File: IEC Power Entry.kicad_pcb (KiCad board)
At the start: 2 copper layers, 64.5 x 70.2 mm, 13 parts, among them J1 Transformer Primary, P1 MountingHole_Pad, P2 Earth

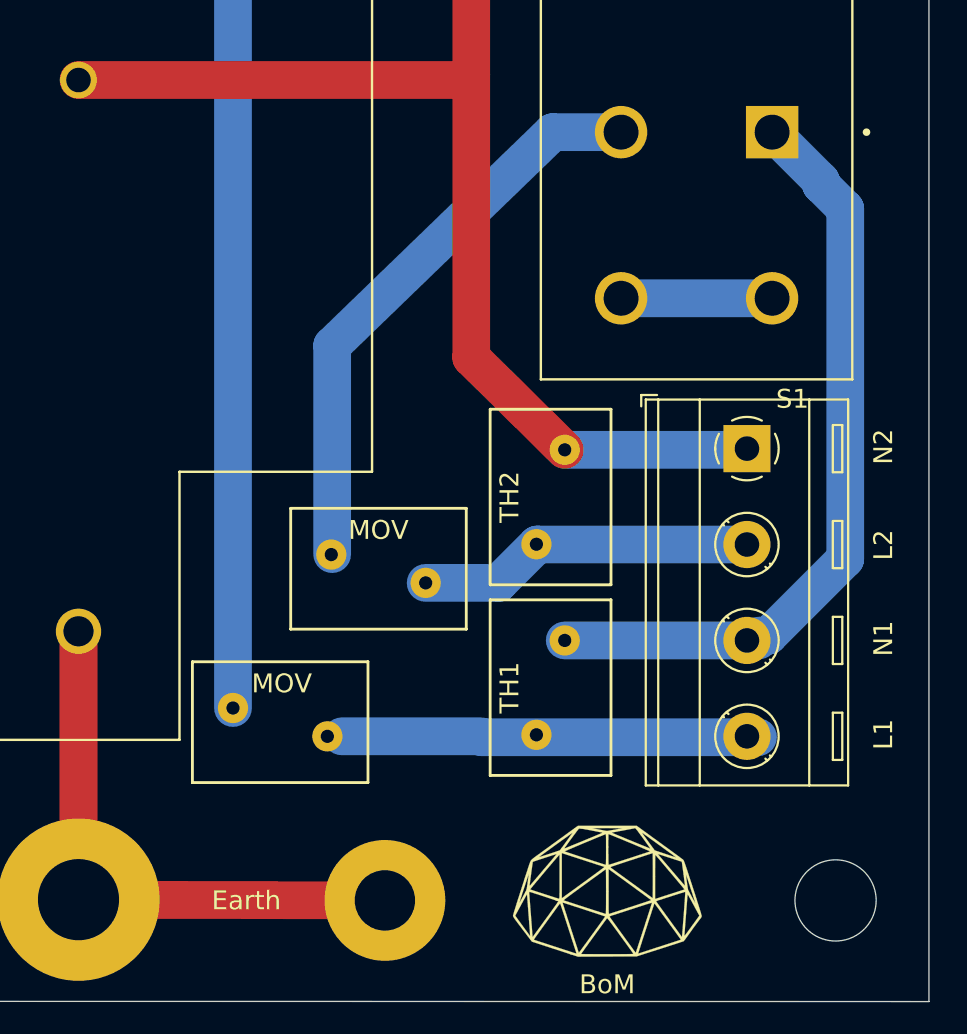
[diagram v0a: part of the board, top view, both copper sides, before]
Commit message: fix: correct mov and inrush placement
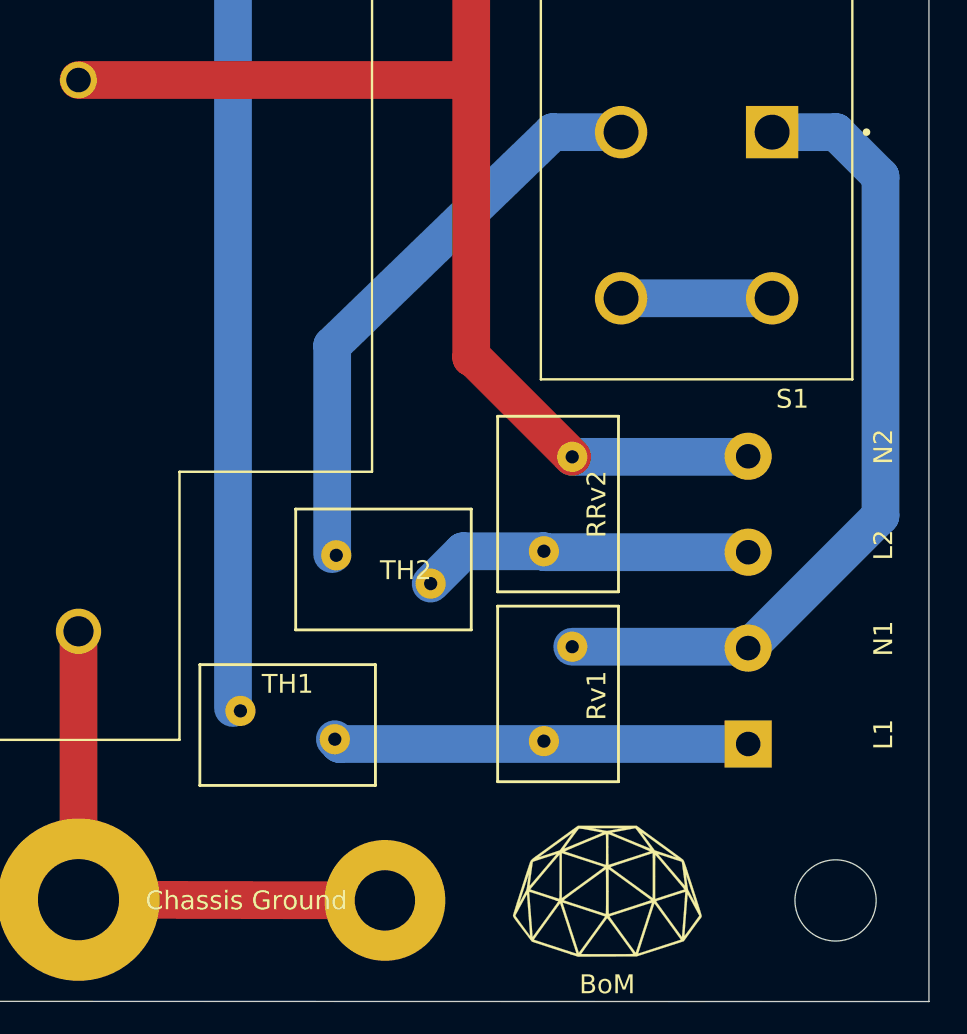
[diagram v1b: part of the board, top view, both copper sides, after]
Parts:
- removed MOV: MOV, Varistor:RV_Disc_D9mm_W6.1mm_P5mm
- added RRv2: MOV, Varistor:RV_Disc_D9mm_W6.1mm_P5mm, F.Cu at (153.4, 109.1)
- J1: moved to B.Cu
- P2: value Earth -> Chassis Ground
- TH1: value Inrush Limiters -> NTC Inrush Limiter
- moved J1 15.6 mm to (164.2, 119.3), turned to 90 degrees
- moved TH2 13.3 mm to (142.4, 109.3), turned to 0 degrees
- moved TH1 13.3 mm to (142.3, 119.0), turned to 180 degrees
- moved Rv1 11.5 mm to (153.4, 119.1), turned to 90 degrees
- renumbered MOV to Rv1
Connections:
- PowerEntry1 pad N: Net-(J1-Pad1) -> Net-(J1-Pad4)
- Rv1 pad 1: Net-(J1-Pad4) -> Net-(J1-Pad1)
- Rv1 pad 2: Net-(PowerEntry1-PadL) -> Net-(J1-Pad2)
- S1 pad 1: Net-(J1-Pad3) -> Net-(J1-Pad2)
- S1 pad 1A: Net-(J1-Pad1) -> Net-(J1-Pad4)
- S1 pad 2: Net-(RRv2-Pad2) -> Net-(S1-Pad2)
- TH1 pad 1: Net-(J1-Pad3) -> Net-(J1-Pad1)
- TH1 pad 2: Net-(J1-Pad4) -> Net-(PowerEntry1-PadL)
- TH2 pad 1: Net-(J1-Pad1) -> Net-(S1-Pad2)
- TH2 pad 2: Net-(J1-Pad2) -> Net-(J1-Pad3)
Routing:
- net Net-(J1-Pad4): track 22.0 -> 85.4 mm
- net Net-(J1-Pad1): track 85.1 -> 22.0 mm
- net Net-(S1-Pad2): track 0.00 -> 30.9 mm
- net Net-(RRv2-Pad2): track 30.9 -> 0.00 mm
- net Net-(J1-Pad2): track 17.9 -> 43.9 mm
- net Net-(J1-Pad3): track 40.4 -> 17.6 mm

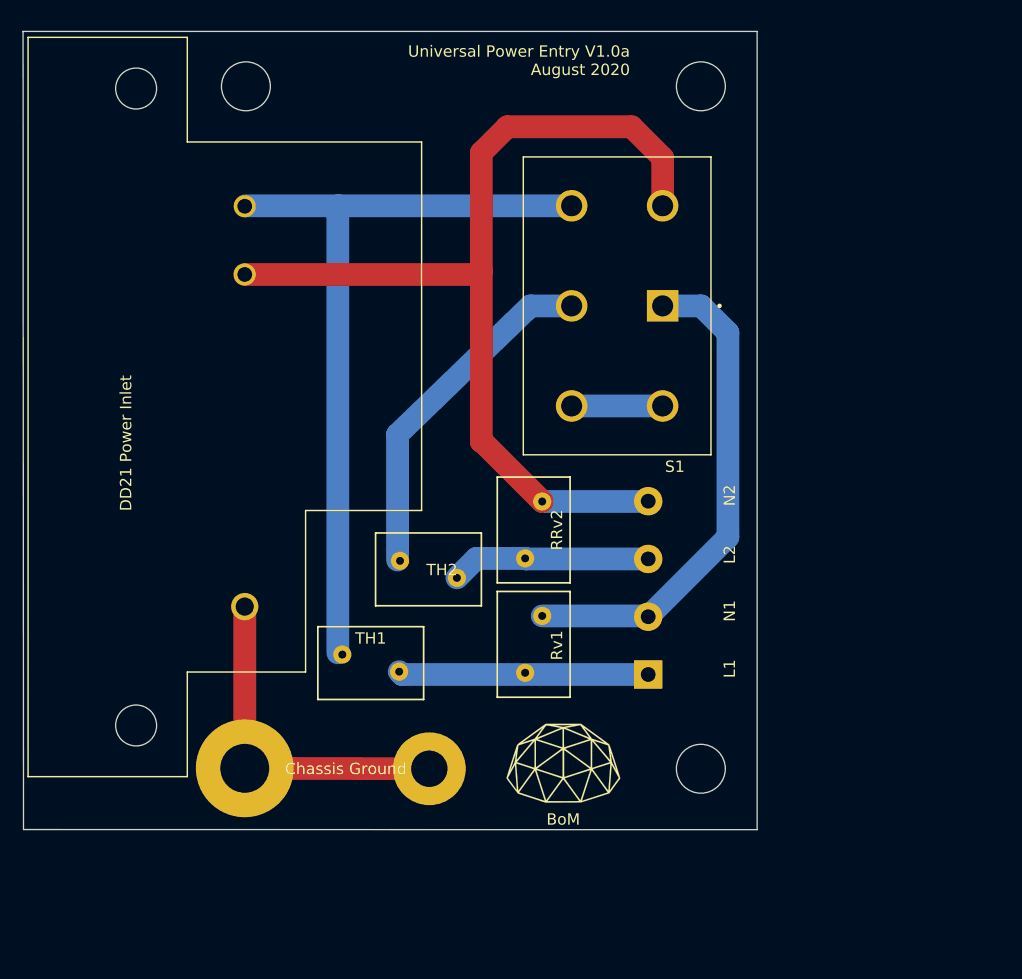
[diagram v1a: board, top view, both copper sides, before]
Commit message: various updates to track widths and footprints
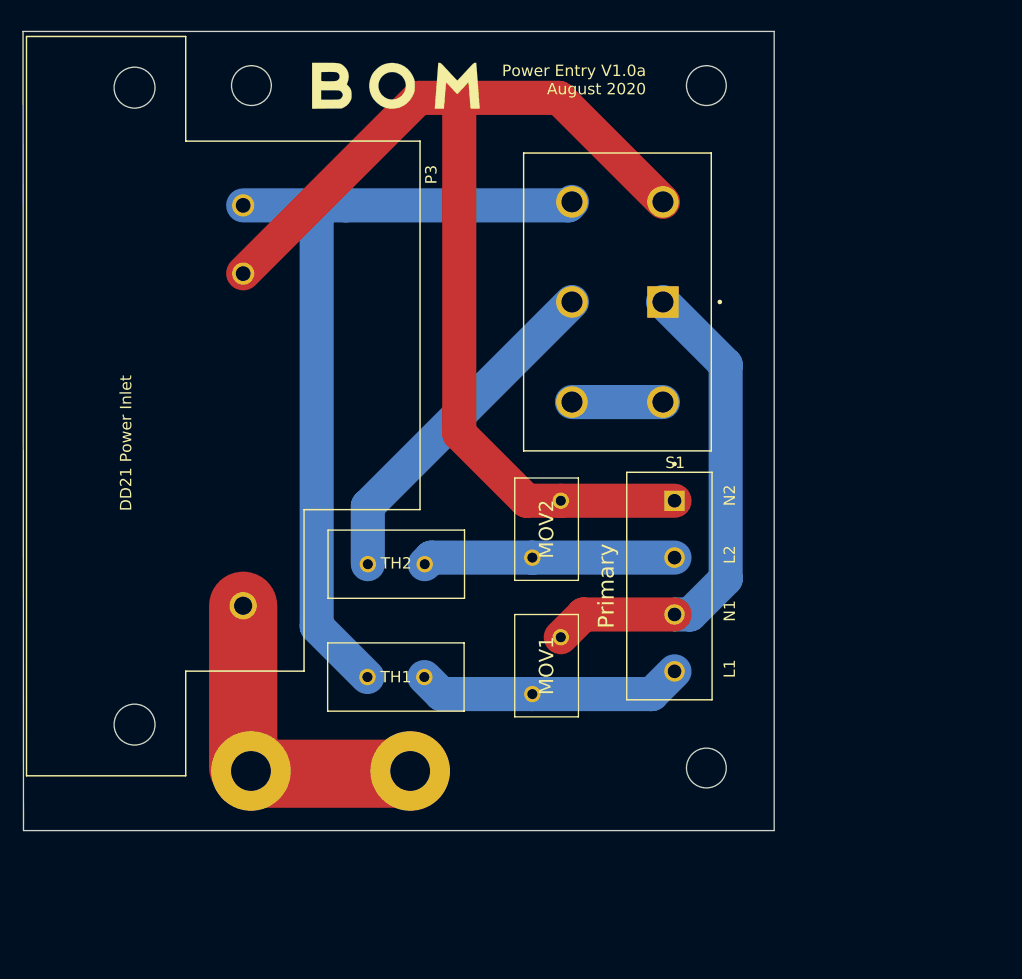
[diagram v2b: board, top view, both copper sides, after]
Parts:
- removed the G*** at (156.7, 127.1)
- removed P1: MountingHole_Pad, MountingHole:MountingHole_4.3mm_M4_Pad
- removed P2: Chassis Ground, MountingHole:MountingHole_3.2mm_M3_Pad
- removed PowerEntry1: DD21, DD21.0121:SCHURTER_DD21.0121.1111
- removed the REF** at (128.8, 67.6)
- removed the REF** at (168.8, 67.6)
- removed the REF** at (168.8, 127.6)
- removed RRv2, Rv1: MOV, Varistor:RV_Disc_D9mm_W6.1mm_P5mm
- added G***: LOGO, Base on Mars Additions:BOM_Simple_14.8x4.1, F.Cu at (142.0, 67.5)
- added MOV1: MOV, Base on Mars Additions:V150LA2PX2855, F.Cu at (154.0, 121.0)
- added MOV2: MOV, Base on Mars Additions:V150LA2PX2855, F.Cu at (154.0, 109.0)
- added P3: DD21.0121.1111, Base on Mars Additions:SCHURTER-DD21.0121.1111, F.Cu at (119.0, 95.7)
- added REF**: MountingHole_3.5mm_Pad, MountingHole:MountingHole_3.5mm_Pad, F.Cu at (129.3, 127.8)
- added REF**: MountingHole_3.5mm_Pad, MountingHole:MountingHole_3.5mm_Pad, F.Cu at (143.3, 127.8)
- added REF**: MountingHole_3.5mm, MountingHole:MountingHole_3.5mm, F.Cu at (129.3, 67.5)
- added REF**: MountingHole_3.5mm, MountingHole:MountingHole_3.5mm, F.Cu at (169.3, 67.5)
- added REF**: MountingHole_3.5mm, MountingHole:MountingHole_3.5mm, F.Cu at (169.3, 127.5)
- J1: value Transformer Primary -> Primary; footprint TerminalBlock_RND:TerminalBlock_RND_205-00289_1x04_P5.08mm_Horizontal -> TerminalBlock_TE-Connectivity:TerminalBlock_TE_1776266-4_1x4_P5mm_Horizonatal; moved to F.Cu
- S1: footprint V80212MS02Q:SW_V80212MS02Q -> Base on Mars Additions:SW_V80212MS02Q
- TH1, TH2: footprint Varistor:RV_Disc_D9mm_W6.1mm_P5mm -> Base on Mars Additions:Thermistor_D8.5mm_W6mm_P5MM
- moved J1 15.5 mm to (166.5, 104.0), turned to 270 degrees
- moved TH1 3.49 mm to (142.0, 122.5)
- moved TH2 2.73 mm to (142.0, 106.6)
- moved S1 0.35 mm to (161.5, 86.5)
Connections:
- S1 pad 1: Net-(J1-Pad2) -> Net-(J1-Pad3)
- S1 pad 1A: Net-(J1-Pad4) -> Net-(J1-Pad1)
- TH1 pad 1: Net-(J1-Pad1) -> Net-(J1-Pad4)
- TH2 pad 2: Net-(J1-Pad3) -> Net-(J1-Pad2)
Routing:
- net Net-(J1-Pad1): track 22.0 -> 98.0 mm
- net Net-(J1-Pad4): track 85.4 -> 23.4 mm
- net Net-(J1-Pad3): track 17.6 -> 43.3 mm
- net Net-(J1-Pad2): track 43.9 -> 22.2 mm
- net Net-(P3-PadL): track 68.0 -> 72.6 mm
- net Net-(P1-Pad1): track 30.5 -> 28.6 mm
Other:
- board size 64.5 x 70.2 mm -> 66 x 70.3 mm
- net class Default: clearance 0.2 -> 1.5; trace_width 0.25 -> 3
- rule trace_clearance: 0.2 -> 1.5
- board text added: "Power Entry V1.0a August 2020"
- board text removed: "BoM"
- board text removed: "Universal Power Entry V1.0a August 2020"

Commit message: chore: increase gaps to meet DIN EN 60664-1 (cat. II) and 230VAC
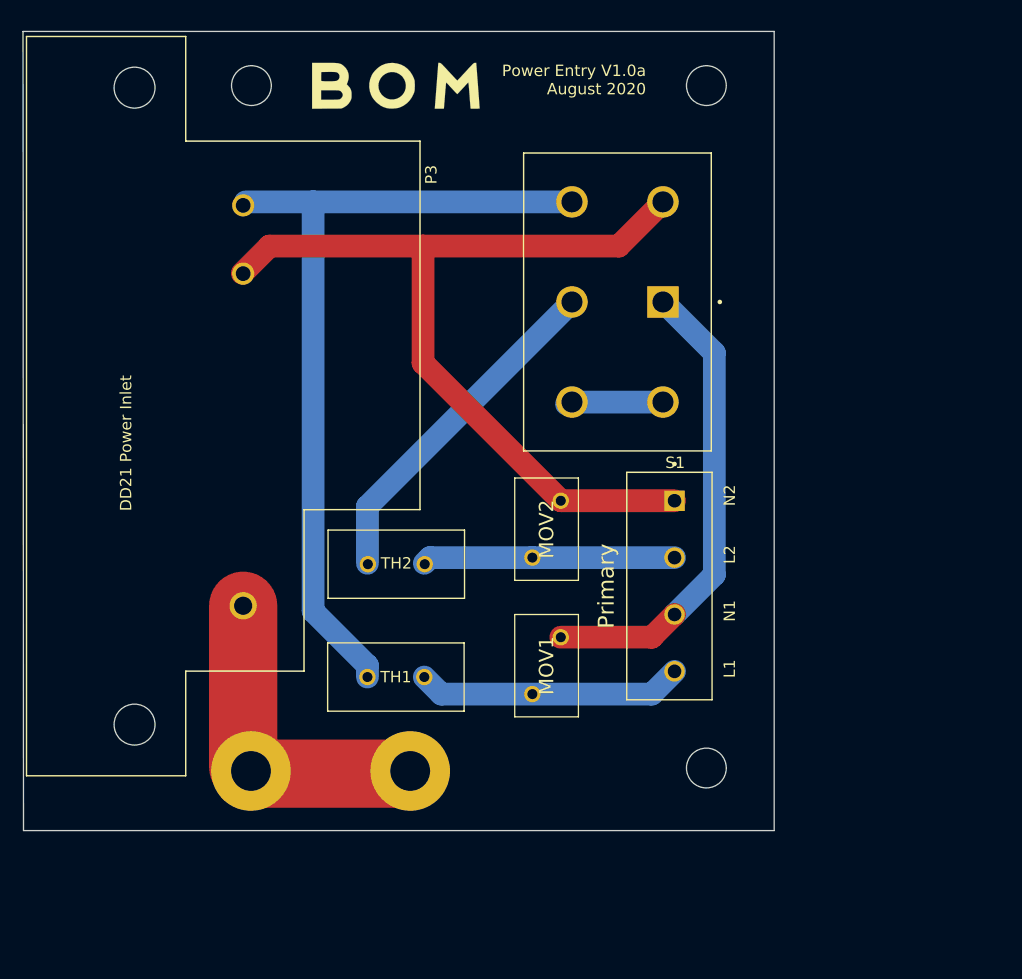
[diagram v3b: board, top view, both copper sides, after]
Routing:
- net Net-(J1-Pad1): track 98.0 -> 77.0 mm
- net Net-(J1-Pad3): track 43.3 -> 41.6 mm
- net Net-(S1-Pad1B): track 8.00 -> 8.55 mm
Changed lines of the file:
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@@
     (thickness 1.6)
     (drawings 10)
-    (tracks 36)
+    (tracks 31)
     (zones 0)
     (modules 13)
@@
   )
   (setup
-    (last_trace_width 6)
+    (last_trace_width 2)
     (user_trace_width 2)
     (user_trace_width 3)
@@
     (effects (font (size 1 1) (thickness 0.15)))
   )
-  (segment (start 146 121) (end 144.5 119.5) (width 3) (layer B.Cu) (net 1))
-  (segment (start 154 121) (end 146 121) (width 3) (layer B.Cu) (net 1))
-  (segment (start 164.5 121) (end 166.5 119) (width 3) (layer B.Cu) (net 1))
-  (segment (start 154 121) (end 164.5 121) (width 3) (layer B.Cu) (net 1))
-  (segment (start 158.5 114) (end 166.5 114) (width 3) (layer F.Cu) (net 2))
-  (segment (start 156.5 116) (end 158.5 114) (width 3) (layer F.Cu) (net 2))
-  (segment (start 167.863975 114) (end 166.5 114) (width 3) (layer B.Cu) (net 2))
-  (segment (start 171.00001 110.863965) (end 167.863975 114) (width 3) (layer B.Cu) (net 2))
-  (segment (start 171.00001 92.04301) (end 171.00001 110.863965) (width 3) (layer B.Cu) (net 2))
-  (segment (start 165.481 86.524) (end 171.00001 92.04301) (width 3) (layer B.Cu) (net 2))
-  (segment (start 145.1152 109) (end 144.5368 109.5784) (width 3) (layer B.Cu) (net 3))
-  (segment (start 154 109) (end 145.1152 109) (width 3) (layer B.Cu) (net 3))
-  (segment (start 154 109) (end 166.5 109) (width 3) (layer B.Cu) (net 3))
-  (segment (start 144.0008 68.58) (end 128.5744 84.0064) (width 3) (layer F.Cu) (net 4))
-  (segment (start 155.956 68.58) (end 147.574 68.58) (width 3) (layer F.Cu) (net 4))
-  (segment (start 147.574 68.58) (end 144.0008 68.58) (width 3) (layer F.Cu) (net 4))
-  (segment (start 156.337 68.58) (end 155.956 68.58) (width 3) (layer F.Cu) (net 4))
-  (segment (start 165.481 77.724) (end 156.337 68.58) (width 3) (layer F.Cu) (net 4))
-  (segment (start 147.574 98.078122) (end 147.574 68.58) (width 3) (layer F.Cu) (net 4))
-  (segment (start 156.5 104) (end 153.495878 104) (width 3) (layer F.Cu) (net 4))
-  (segment (start 153.495878 104) (end 147.574 98.078122) (width 3) (layer F.Cu) (net 4))
-  (segment (start 166.5 104) (end 156.5 104) (width 3) (layer F.Cu) (net 4))
+  (segment (start 166.5 119) (end 164.5 121) (width 2) (layer B.Cu) (net 1))
+  (segment (start 164.5 121) (end 146 121) (width 2) (layer B.Cu) (net 1))
+  (segment (start 146 121) (end 144.5 119.5) (width 2) (layer B.Cu) (net 1))
+  (segment (start 170.00001 110.49999) (end 170.00001 91.00001) (width 2) (layer B.Cu) (net 2))
+  (segment (start 166.5 114) (end 170.00001 110.49999) (width 2) (layer B.Cu) (net 2))
+  (segment (start 170.00001 91.00001) (end 165.5 86.5) (width 2) (layer B.Cu) (net 2))
+  (segment (start 156.5 116) (end 164.5 116) (width 2) (layer F.Cu) (net 2))
+  (segment (start 164.5 116) (end 166.5 114) (width 2) (layer F.Cu) (net 2))
+  (segment (start 166.5 109) (end 154 109) (width 2) (layer B.Cu) (net 3))
+  (segment (start 154 109) (end 145 109) (width 2) (layer B.Cu) (net 3))
+  (segment (start 145 109) (end 144.5 109.5) (width 2) (layer B.Cu) (net 3))
+  (segment (start 165.481 77.724) (end 161.593499 81.611501) (width 2) (layer F.Cu) (net 4))
+  (segment (start 130.888499 81.611501) (end 128.5 84) (width 2) (layer F.Cu) (net 4))
+  (segment (start 166.5 104) (end 156.5 104) (width 2) (layer F.Cu) (net 4))
+  (segment (start 144.388499 91.888499) (end 144.388499 81.611501) (width 2) (layer F.Cu) (net 4))
+  (segment (start 144.388499 81.611501) (end 130.888499 81.611501) (width 2) (layer F.Cu) (net 4))
+  (segment (start 156.5 104) (end 144.388499 91.888499) (width 2) (layer F.Cu) (net 4))
+  (segment (start 161.593499 81.611501) (end 144.388499 81.611501) (width 2) (layer F.Cu) (net 4))
   (segment (start 128.5744 113.2318) (end 128.5744 127.4256) (width 6) (layer F.Cu) (net 5))
   (segment (start 143.26 127.76) (end 143.26 127.74) (width 6) (layer F.Cu) (net 5))
   (segment (start 143.26 127.74) (end 143 128) (width 6) (layer F.Cu) (net 5))
   (segment (start 143 128) (end 129 128) (width 6) (layer F.Cu) (net 5))
-  (segment (start 165.481 95.324) (end 157.481 95.324) (width 3) (layer B.Cu) (net 6))
-  (segment (start 139.5368 104.4682) (end 139.5368 109.5784) (width 3) (layer B.Cu) (net 7))
-  (segment (start 157.481 86.524) (end 139.5368 104.4682) (width 3) (layer B.Cu) (net 7))
-  (segment (start 157.1732 78.0318) (end 157.481 77.724) (width 3) (layer B.Cu) (net 8))
-  (segment (start 137.5948 78.0318) (end 157.1732 78.0318) (width 3) (layer B.Cu) (net 8))
-  (segment (start 134.4682 78.0318) (end 137.5948 78.0318) (width 3) (layer B.Cu) (net 8))
-  (segment (start 128.5744 78.0318) (end 134.4682 78.0318) (width 3) (layer B.Cu) (net 8))
-  (segment (start 135.03679 78.60039) (end 134.4682 78.0318) (width 3) (layer B.Cu) (net 8))
-  (segment (start 135.03679 115.03679) (end 135.03679 78.60039) (width 3) (layer B.Cu) (net 8))
-  (segment (start 139.5 119.5) (end 135.03679 115.03679) (width 3) (layer B.Cu) (net 8))
+  (segment (start 165.481 95.324) (end 157.176 95.324) (width 2) (layer B.Cu) (net 6))
+  (segment (start 157.176 95.324) (end 157 95.5) (width 2) (layer B.Cu) (net 6))
+  (segment (start 157.481 86.524) (end 139.5 104.505) (width 2) (layer B.Cu) (net 7))
+  (segment (start 139.5 104.505) (end 139.5 109.5) (width 2) (layer B.Cu) (net 7))
+  (segment (start 134.724 113.707181) (end 134.724 77.724) (width 2) (layer B.Cu) (net 8))
+  (segment (start 139.5 118.483181) (end 134.724 113.707181) (width 2) (layer B.Cu) (net 8))
+  (segment (start 139.5 119.5) (end 139.5 118.483181) (width 2) (layer B.Cu) (net 8))
+  (segment (start 134.724 77.724) (end 128.776 77.724) (width 2) (layer B.Cu) (net 8))
+  (segment (start 157.481 77.724) (end 134.724 77.724) (width 2) (layer B.Cu) (net 8))
 )
